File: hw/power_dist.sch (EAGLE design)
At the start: 98 parts, among them J1 JST-ZH6SMT_VERT, J2 JST-PH4SMT_VERT, J3 JST-PH5VERT, P1 XT30P, P2 XT30P, P3 XT30P, P4 XT30P, P5 XT30P, P6 XT30P, P7 XT90PW-M, Q1 PSMN4R8-100BSEJ, Q2 PSMN4R8-100BSEJ, Q3 PSMN4R8-100BSEJ, Q4 MF-DSC-SOT233-MMBT3904, Q5 MMBT5401 100V, U1 MAX15062AATA+T, U2 STM32G474CEU6, U3 TPS2490DGSR, U4 TCAN334G, U5 LT1787HVIMS8PBF, U6 STLM20DD9FUDFN-4L_STM-L

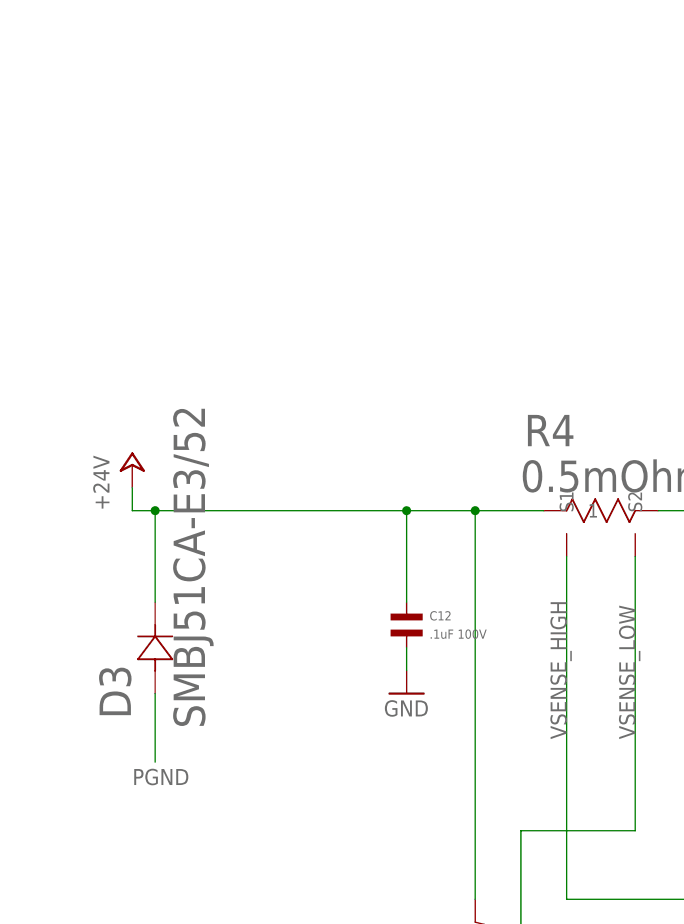
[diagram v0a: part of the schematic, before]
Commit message: Tweak silks and layouts, set isolate for all power nets
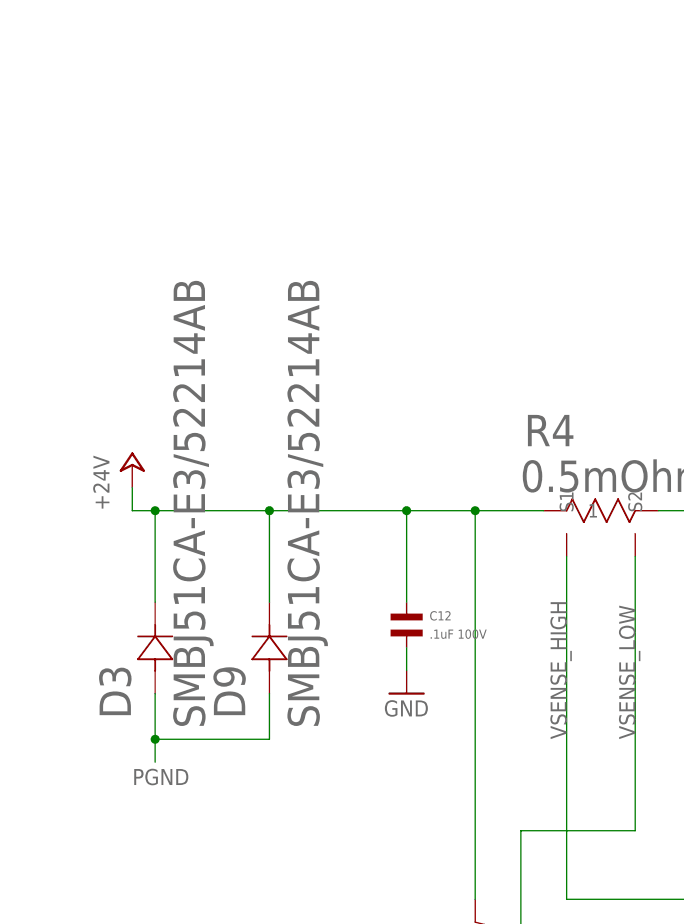
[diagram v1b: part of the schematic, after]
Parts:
- added D9: SMBJ51CA-E3/52214AB, power_dist:SMBJ51CA-E3/52214AB
- D3: value SMBJ51CA-E3/52 -> SMBJ51CA-E3/52214AB; device power_dist:SMBJ51CA-E3/52 -> power_dist:SMBJ51CA-E3/52214AB; MPN SMBJ51CA-E3/52 -> SMC5K51A-M3/I
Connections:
- net +24V: now also D9.1
- net PGND: now also D9.2
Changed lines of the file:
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@@
 <part name="P+5" library="supply1" library_urn="urn:adsk.eagle:library:371" deviceset="+24V" device=""/>
 <part name="GND6" library="supply1" deviceset="GND" device=""/>
-<part name="D3" library="power_dist" deviceset="SMBJ51CA-E3/52" device="">
-<attribute name="MPN" value="SMBJ51CA-E3/52"/>
+<part name="D3" library="power_dist" deviceset="SMBJ51CA-E3/52" device="214AB" value="SMBJ51CA-E3/52214AB">
+<attribute name="MPN" value="SMC5K51A-M3/I"/>
 <attribute name="POPULATE" value="1"/>
 </part>
@@
 <part name="R26" library="mfpassives" deviceset="RESISTOR" device="_0603" value="0">
 <attribute name="HOUSEPART" value="1"/>
+</part>
+<part name="D9" library="power_dist" deviceset="SMBJ51CA-E3/52" device="214AB" value="SMBJ51CA-E3/52214AB">
+<attribute name="MPN" value="SMC5K51A-M3/I"/>
+<attribute name="POPULATE" value="1"/>
 </part>
 </parts>
@@
 <attribute name="VALUE" x="399.796" y="129.54" size="1.016" layer="96" font="vector" rot="R270"/>
 </instance>
+<instance part="D9" gate="A" x="-50.8" y="7.62" smashed="yes" rot="R90">
+<attribute name="VALUE" x="-45.2628" y="3.7338" size="3.4798" layer="96" ratio="10" rot="SR90"/>
+<attribute name="NAME" x="-53.4924" y="4.8006" size="3.4798" layer="95" ratio="10" rot="SR90"/>
+<attribute name="MPN" x="-50.8" y="7.62" size="1.778" layer="96" rot="R90" display="off"/>
+<attribute name="POPULATE" x="-50.8" y="7.62" size="1.778" layer="96" rot="R90" display="off"/>
+</instance>
 </instances>
 <busses>
@@
 <junction x="-63.5" y="27.94"/>
 <pinref part="R4" gate="A" pin="1"/>
-<wire x1="-63.5" y1="27.94" x2="-35.56" y2="27.94" width="0.1524" layer="91"/>
+<wire x1="-63.5" y1="27.94" x2="-50.8" y2="27.94" width="0.1524" layer="91"/>
 <pinref part="R3" gate="G$1" pin="P$2"/>
+<wire x1="-50.8" y1="27.94" x2="-35.56" y2="27.94" width="0.1524" layer="91"/>
 <wire x1="-35.56" y1="27.94" x2="-27.94" y2="27.94" width="0.1524" layer="91"/>
 <wire x1="-27.94" y1="27.94" x2="-20.32" y2="27.94" width="0.1524" layer="91"/>
@@
 <wire x1="-35.56" y1="17.78" x2="-35.56" y2="27.94" width="0.1524" layer="91"/>
 <junction x="-35.56" y="27.94"/>
+<pinref part="D9" gate="A" pin="1"/>
+<wire x1="-50.8" y1="17.78" x2="-50.8" y2="27.94" width="0.1524" layer="91"/>
+<junction x="-50.8" y="27.94"/>
 </segment>
 <segment>
@@
 <segment>
 <pinref part="D3" gate="A" pin="2"/>
-<wire x1="-63.5" y1="7.62" x2="-63.5" y2="0" width="0.1524" layer="91"/>
+<wire x1="-63.5" y1="7.62" x2="-63.5" y2="2.54" width="0.1524" layer="91"/>
 <label x="-66.04" y="-2.54" size="1.778" layer="95"/>
-</segment>
-<segment>
+<pinref part="D9" gate="A" pin="2"/>
+<wire x1="-63.5" y1="2.54" x2="-63.5" y2="0" width="0.1524" layer="91"/>
+<wire x1="-63.5" y1="2.54" x2="-50.8" y2="2.54" width="0.1524" layer="91"/>
+<wire x1="-50.8" y1="2.54" x2="-50.8" y2="7.62" width="0.1524" layer="91"/>
+<junction x="-63.5" y="2.54"/>
+</segment>
+<segment>

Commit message: Update the solder mask to be more amenable to oshstencil
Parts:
- U2: device precharge:STM32G474CEU6 -> power_dist:STM32G474CEU6
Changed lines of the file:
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@@
 <attribute name="POPULATE" value="1"/>
 </part>
-<part name="U2" library="precharge" deviceset="STM32G474CEU6" device="">
+<part name="U2" library="power_dist" deviceset="STM32G474CEU6" device="">
 <attribute name="MF" value="ST"/>
 <attribute name="MPN" value="STM32G474CEU6"/>

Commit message: Fix a part number
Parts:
- C12: MPN MF-CAP-0603-0.1uF -> GRM188R72A104KA35D
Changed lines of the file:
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@@
 <part name="C12" library="mfpassives" deviceset="CAPACITOR_NP" device="_0603" value=".1uF 100V">
 <attribute name="HOUSEPART" value="1"/>
-<attribute name="MPN" value="MF-CAP-0603-0.1uF"/>
+<attribute name="MPN" value="GRM188R72A104KA35D"/>
 </part>
 <part name="GND7" library="supply1" deviceset="GND" device=""/>

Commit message: Start on r4.3
This version dispenses with all the latching junk for main power, just
leaving it for the 3.3V rail.  Now, the stm32 is completely
responsible for turning the main power on and off, which could allow
it to reset the hot swap controller if need be.
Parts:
- removed D6, D7: MF-DIO-SOD123-1N4148, mfdiscretesemi:DIODES_1N4148_SOD-123
- removed Q4: MF-DSC-SOT233-MMBT3904, mfdiscretesemi:NPN_BJTMMBT3904_SOT-23-3
- removed Q5: MMBT5401 100V, mfdiscretesemi:PNP_BJT_MMBT3906_SOT-23-3
- removed R18: 2M, mfpassives:RESISTOR_0603
- removed R19: 200k, mfpassives:RESISTOR_0603
- removed R20: 100k, mfpassives:RESISTOR_0603
- removed R22: DNP, mfpassives:RESISTOR_0603
- removed R23: 33k, mfpassives:RESISTOR_0603
- C12: MPN GRM188R72A104KA35D -> MF-CAP-0603-0.1uF
- R16: value 1k -> 200k 1%
- R17: value 500k -> 200k 1%
- R3: value 2M -> 200k 1%
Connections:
- removed net LTC_EN: DB_LEN.P$1, Q5.EMITTER, R3.P$1, U3.EN
- removed net N$11: Q4.BASE, R18.P$1, R22.P$2
- removed net N$13: D6.CATHODE, D7.CATHODE, Q5.BASE, R19.P$2
- removed net N$17: D6.ANODE, R17.P$1
- removed net N$18: D7.ANODE, R16.P$1
- removed net PWR_OVERRIDE: R16.P$2, U2.PC14-OSC32_IN
- new net TPS_EN: DB_LEN.P$1, R16.P$2, U2.PC14-OSC32_IN, U3.EN
- net +24V: no longer R3.P$2
- net GND: now also R16.P$1, R17.P$2; no longer Q4.EMITTER, Q5.COLLECTOR, R19.P$1, R20.P$1, R22.P$1
- net PWR_SW: now also R3.P$2; no longer R17.P$2, R18.P$2, R20.P$2
- net SNS_PWR_SW: now also R17.P$1, R3.P$1; no longer Q4.COLLECTOR, R23.P$1
- net VCC: no longer R23.P$2
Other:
- note added: "mjbots power dist r4.3 (c) 2020 Josh Pieper, jjp@pobox.com Licensed under the Apache 2.0 License https://www.apache.org/licenses/LICENSE-2.0"
- note removed: "This circuit exists to keep the TPS disabled until the switch is closed, but also to draw minimal quiescent current both while it is disabled, and while the switch is closed and the TPS controller is enabled. Also, it supports the microcontroller latching the TPS on, while still being able to monitor the state of the actual power switch."
- note removed: "mjbots power dist r4.2 (c) 2020 Josh Pieper, jjp@pobox.com Licensed under the Apache 2.0 License https://www.apache.org/licenses/LICENSE-2.0"
- moved on the sheet: C5, R16, R17, R21, R3

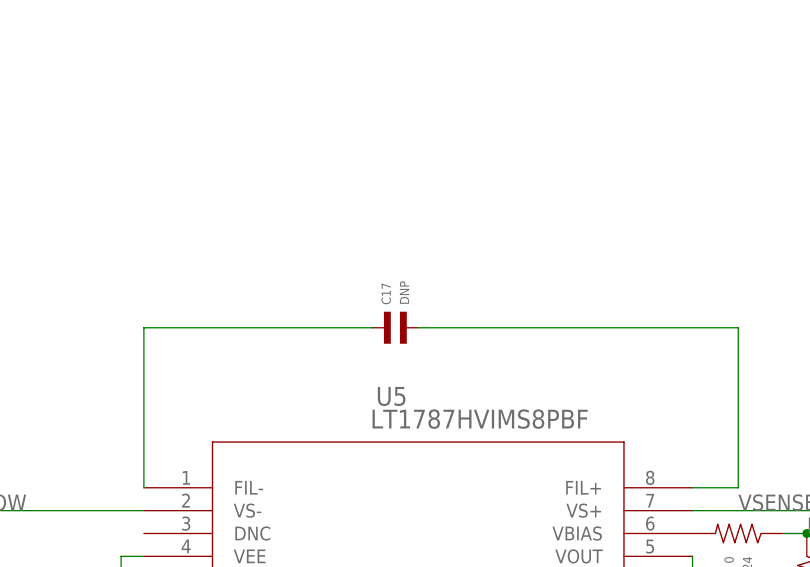
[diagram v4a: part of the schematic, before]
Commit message: Switch the LTC1787 filter to a 0.1uF
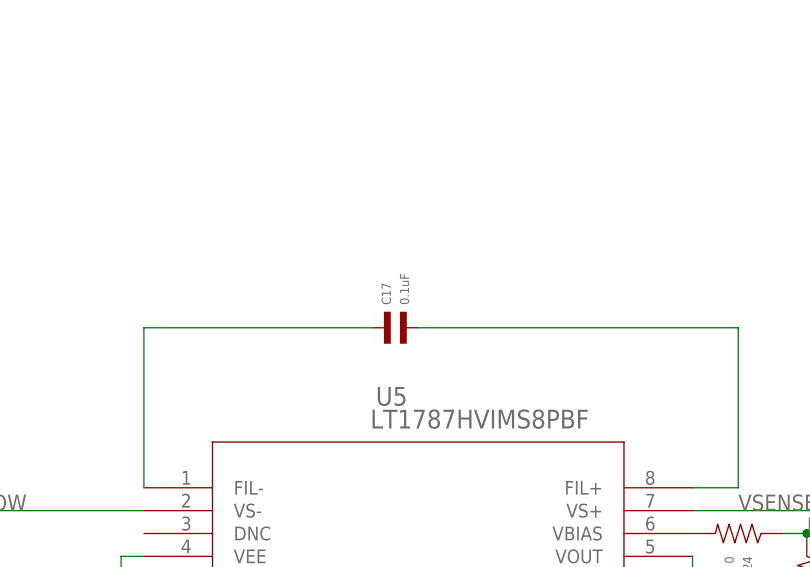
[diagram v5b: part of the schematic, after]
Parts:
- C17: value DNP -> 0.1uF; HOUSEPART (none) -> 1; MPN (none) -> MF-CAP-0603-0.1uF; POPULATE 0 -> (none)
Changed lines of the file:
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@@
 <part name="U5" library="LT1787HVIMS8PBF" deviceset="LT1787HVIMS8PBF" device=""/>
 <part name="GND10" library="supply1" deviceset="GND" device=""/>
-<part name="C17" library="mfpassives" deviceset="CAPACITOR_NP" device="_0603" value="DNP">
-<attribute name="POPULATE" value="0"/>
+<part name="C17" library="mfpassives" deviceset="CAPACITOR_NP" device="_0603" value="0.1uF">
+<attribute name="HOUSEPART" value="1"/>
+<attribute name="MPN" value="MF-CAP-0603-0.1uF"/>
 </part>
 <part name="C20" library="mfpassives" deviceset="CAPACITOR_NP" device="_0603" value="0.1uF">

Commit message: Updates for r4.3
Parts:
- added D6: 3V ZENER, mfdiscretesemi:DIODES_1N4148_SOD-123
- added Q4: (no value), mfdiscretesemi:N-CHANNEL_FET_SOT-23-3
- added Q5: (no value), mfdiscretesemi:P-CHANNEL_FET_SOT-23-3
- added R18: 100k 1%, mfpassives:RESISTOR_0603
- added R19: 499k 1%, mfpassives:RESISTOR_0603
- added R20: 47k 1%, mfpassives:RESISTOR_0603
- added R22: 200k 1%, mfpassives:RESISTOR_0603
- R16: value 200k 1% -> 100k
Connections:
- new net N$11: Q5.DRAIN, R19.P$2
- new net N$12: R18.P$2, R19.P$1, U3.EN
- new net N$13: Q4.DRAIN, R22.P$1
- new net N$16: Q5.GATE, R20.P$1, R22.P$2
- net +24V: now also Q5.SOURCE, R20.P$2
- net GND: now also D6.ANODE, Q4.SOURCE, R18.P$1
- net SNS_PWR_SW: now also D6.CATHODE
- net TPS_EN: now also Q4.GATE; no longer U3.EN
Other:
- moved on the sheet: R16, R17, R3
